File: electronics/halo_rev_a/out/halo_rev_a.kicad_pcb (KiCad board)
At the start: 4 copper layers, 25.6 x 26 mm, 62 parts, among them J1 TC2030, J2 UWB stub, U1 nRF54L10-QFAA-R7, U2 LIS2DW12TR, X1 32.768kHz, X2 32MHz

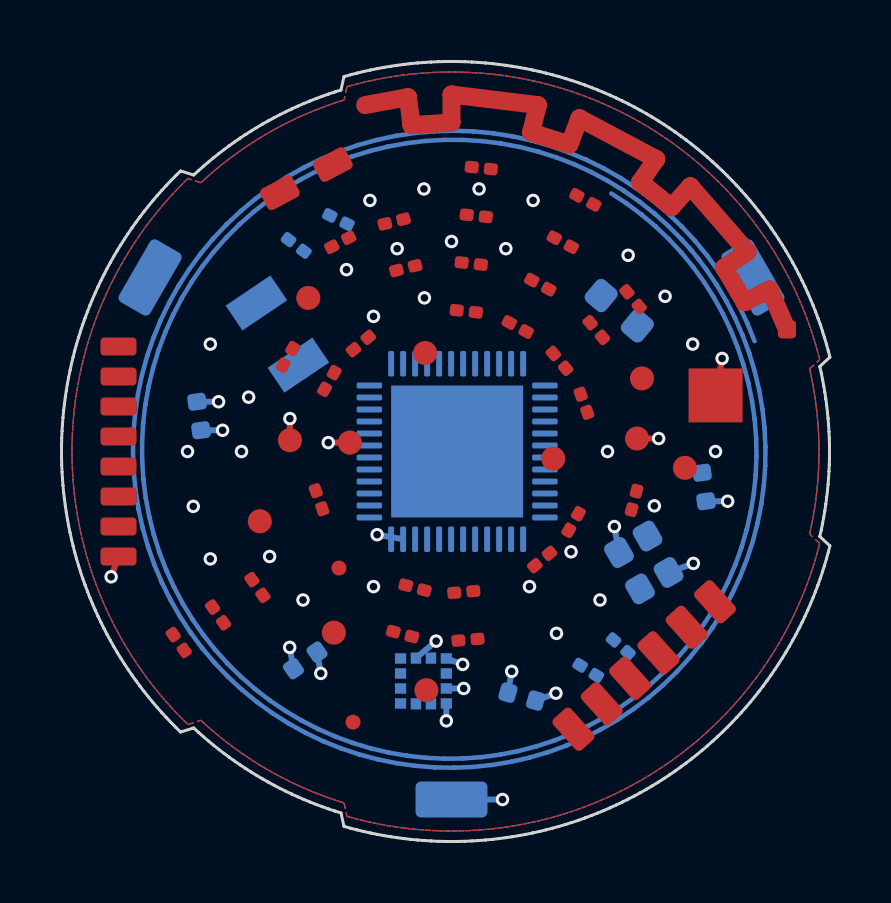
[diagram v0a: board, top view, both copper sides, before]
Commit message: B1: nine meander teeth take the NFC coil out from under the antenna arm
The coil overlapped the 2.4 GHz arm by 0.1747 mm. Lane T3 measured what that
costs: coil under the arm 1.7666 GHz against 2.4346 GHz clear, a 668 MHz shift
no tuning recovers. Fixed in the copper, and the fix is free in the one
dimension that matters.

WHY THE BAND WOULD NOT CLOSE ANY OTHER WAY. The coil lives between the cell
can at R10.00 (copper over a steel can is a shorted turn) and the arm's inner
copper edge. At 4 teeth the arm needs a depth of 0.9379 mm, which puts that
edge at R10.6621 and leaves the coil 0.6621 mm for the 0.782 mm it needs — a
0.4197 mm shortfall it was taking by lying under the arm. Every other lever is
too small: moving the arm out is 0.050 mm before the R12.25 notch cap,
narrowing it 0.60->0.40 is 0.100 mm, a 0.127 mm coil trace is 0.120 mm. Only
cutting the coil's turns closes it, and that costs inductance the NFC tank
cannot spare.

THE TOOTH COUNT WAS THE FREE VARIABLE NOBODY HAD SWEPT, and it is free where
it counts: the bisection holds the conductor at exactly QUARTER_MM whatever
the count, so the length that sets the resonance does not move. Depth falls
as roughly 1/teeth.

    teeth  depth    arm inner R   gap to coil
      4    0.9379     10.6621       -0.1197   overlapping
      6    0.6253     10.9747       +0.1929
      8    0.4614     11.1386       +0.3567   first count that clears
      9    0.4080     11.1977       +0.4158   shipped

Eight is the first count that clears T3's 0.30 mm floor and NINE is shipped:
eight measured 0.3096 mm on the real drawn copper, 9.6 um above the floor,
which is inside JLCPCB's own +/-20 % track-width tolerance and so is not a
margin. Nine measures 0.3627 mm. The coil cannot buy that from the other
side — its inner copper edge is already R10.043 against the can at R10.00.

The tooth SLOT FRACTION had to change too, and checking it caught a defect
before it shipped: the two radial walls of one tooth are `w` apart at their
c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
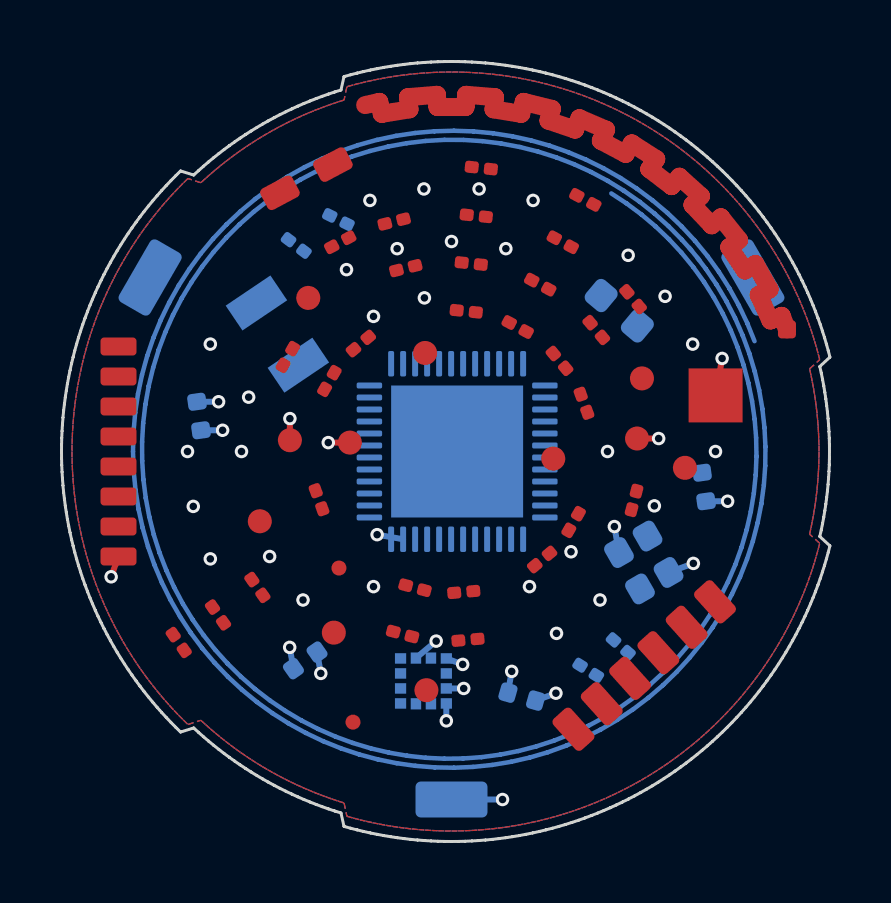
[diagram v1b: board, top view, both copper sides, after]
